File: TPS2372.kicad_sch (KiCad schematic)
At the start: 29 parts

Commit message: tps2372 finish
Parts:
- added C? (x4): 1nF, symbol Device:C
- added C?: 0.1uF, symbol Device:C
- added C?: 100uF, symbol Device:C_Polarized
- added C?: 47uF, symbol Device:C_Polarized
- added D?: 58V, symbol Device:D_TVS
- added D? (x3): Yellow, symbol Device:LED_Small
- added D?: D, symbol Device:D
- added D?: 100V, symbol Device:D_Schottky
- added D?: 12V, symbol Device:D_Zener
- added FB? (x4): 300ohm@100MHz, symbol Device:FerriteBead
- added J? (x3): Conn_01x02, TestPoint:TestPoint_2Pads_Pitch2.54mm_Drill0.8mm, symbol Connector_Generic:Conn_01x02
- added J?: Conn_01x03, symbol Connector_Generic:Conn_01x03
- added J?: Conn_02x05_Odd_Even, symbol Connector_Generic:Conn_02x05_Odd_Even
- added J?: Conn_02x02_Odd_Even, symbol Connector_Generic:Conn_02x02_Odd_Even
- added J?: Screw_Terminal_01x02, symbol Connector:Screw_Terminal_01x02
- added J?: Conn_01x02, symbol Connector_Generic:Conn_01x02
- added L? (x2): L_Coupled_1243, symbol Device:L_Coupled_1243
- added R?: 249, symbol Device:R
- added R?: 24.9k, symbol Device:R
- added R? (x3): 21k, symbol Device:R_Small
- added R? (x2): 49.9k, symbol Device:R
- added R?: 1k, symbol Device:R
- added R? (x2): 20k, symbol Device:R
- added R? (x2): 90.9, symbol Device:R
- added R?: 140, symbol Device:R
- added R? (x2): 63.4, symbol Device:R
- added R?: 53.6k, symbol Device:R
- added R?: 1.21k, symbol Device:R
- added RV?: 2k, symbol Device:R_Potentiometer
- added TP?: VSSA, symbol Connector:TestPoint
- added TP?: +48 Test 2, symbol Connector:TestPoint
- added TP?: AMPS_CTL, symbol Connector:TestPoint
- added TP? (x4): TestPoint, symbol Connector:TestPoint
- added TP?: RTN, symbol Connector:TestPoint
- added TP?: +48 Test 1, symbol Connector:TestPoint
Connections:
- net +48V: now also U?.1 (VDD), C?.1, C?.1, C?.1, C?.1, D?.1 (A1), D?.1 (K), FB?.2, L?.1, R?.1, R?.1, R?.2, R?.2, R?.2, TP?.1, TP?.1
- net BR_OFF: now also R?.1, R?.2
- net TCTA: now also C?.1, FB?.1, L?.2
- net TCTC: now also C?.2, FB?.1, L?.3
- net at U?.10 (AUTCLS_N): now also J?.1 (Pin_1)
- net PoE_RTN: now reaches U?.11 (RTN)
- net PoE_RTN: now also U?.12 (RTN), C?.2, C?.2, C?.2, D?.1 (K), FB?.2, J?.2 (Pin_2), L?.4, TP?.1
- net at U?.13 (PG): now also R?.2, TP?.1
- net at U?.16 (IRSHDL_EN): now also J?.1 (Pin_1)
- net at U?.17 (TPL): now also D?.1 (K), TP?.1
- net at U?.18 (TPH): now also D?.1 (K), TP?.1
- net at U?.19 (BT_N): now also D?.1 (K), TP?.1
- net at U?.2 (DEN): now also R?.2
- net at U?.21 (VSS): now also U?.4 (VSS), U?.5 (VSS), C?.2, J?.1 (Pin_1), J?.1 (Pin_1), J?.2 (Pin_2), J?.2 (Pin_2), J?.2 (Pin_2), J?.3 (Pin_3), J?.3 (Pin_3), J?.3 (Pin_3), J?.5 (Pin_5), J?.7 (Pin_7), J?.9 (Pin_9), R?.2, R?.2
- net at U?.3 (CLSA): now also R?.1, R?.1
- net at U?.6 (CLSB): now also R?.1, R?.1, R?.1, R?.1, R?.1
- net at U?.7 (REF): now also R?.1
- net at U?.8 (AMPS_CTL): now also R?.1, TP?.1
- net at U?.9 (MPS_DUTY): now also J?.2 (Pin_2)
- net at U?.5 (OUTP), U?.6 (OUTP), U?.7 (OUTP)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: no longer U?.5 (OUTP), U?.6 (OUTP), U?.7 (OUTP), U?.8 (OUTP)
- new net: J?.6 (Pin_6), R?.2
- new net: C?.2, FB?.1, J?.2 (Pin_2), L?.3
- new net: D?.2 (A), R?.1 (x4)
- new net: J?.1 (Pin_1), RV?.2
- new net: R?.2, RV?.3
- new net: J?.1 (Pin_1), R?.1
- new net: C?.1, D?.1 (K), D?.2 (A), FB?.2, L?.1
- new net: C?.1, FB?.1, J?.1 (Pin_1), L?.2
- new net: U?.5 (OUTP), U?.6 (OUTP), U?.7 (OUTP), U?.8 (OUTP)
- new net: J?.10 (Pin_10), R?.2
- new net: J?.2 (Pin_2), R?.2 (x2)
- new net: J?.4 (Pin_4), R?.2 (x2)
- new net: J?.8 (Pin_8), R?.2
- new net: D?.2 (A), R?.2
- new net VSSA: C?.2, D?.2 (A2), FB?.2, J?.1 (Pin_1), L?.4, TP?.1
- no-connect marks 0 -> 3
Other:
- note added: "4-Pair"
- note added: "Class 4 Class 3"
- note added: "Class 8 Class 7 Class 6 Class 5 Class 4"
- moved on the sheet: U?

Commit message: buck converter init
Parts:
- J?: footprint (none) -> TestPoint:TestPoint_2Pads_Pitch2.54mm_Drill0.8mm
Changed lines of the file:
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@@
       (effects (font (size 1.27 1.27)) (justify right))
     )
-    (property "Footprint" "" (id 2) (at 41.91 234.95 0)
+    (property "Footprint" "TestPoint:TestPoint_2Pads_Pitch2.54mm_Drill0.8mm" (id 2) (at 41.91 234.95 0)
       (effects (font (size 1.27 1.27)) hide)
     )

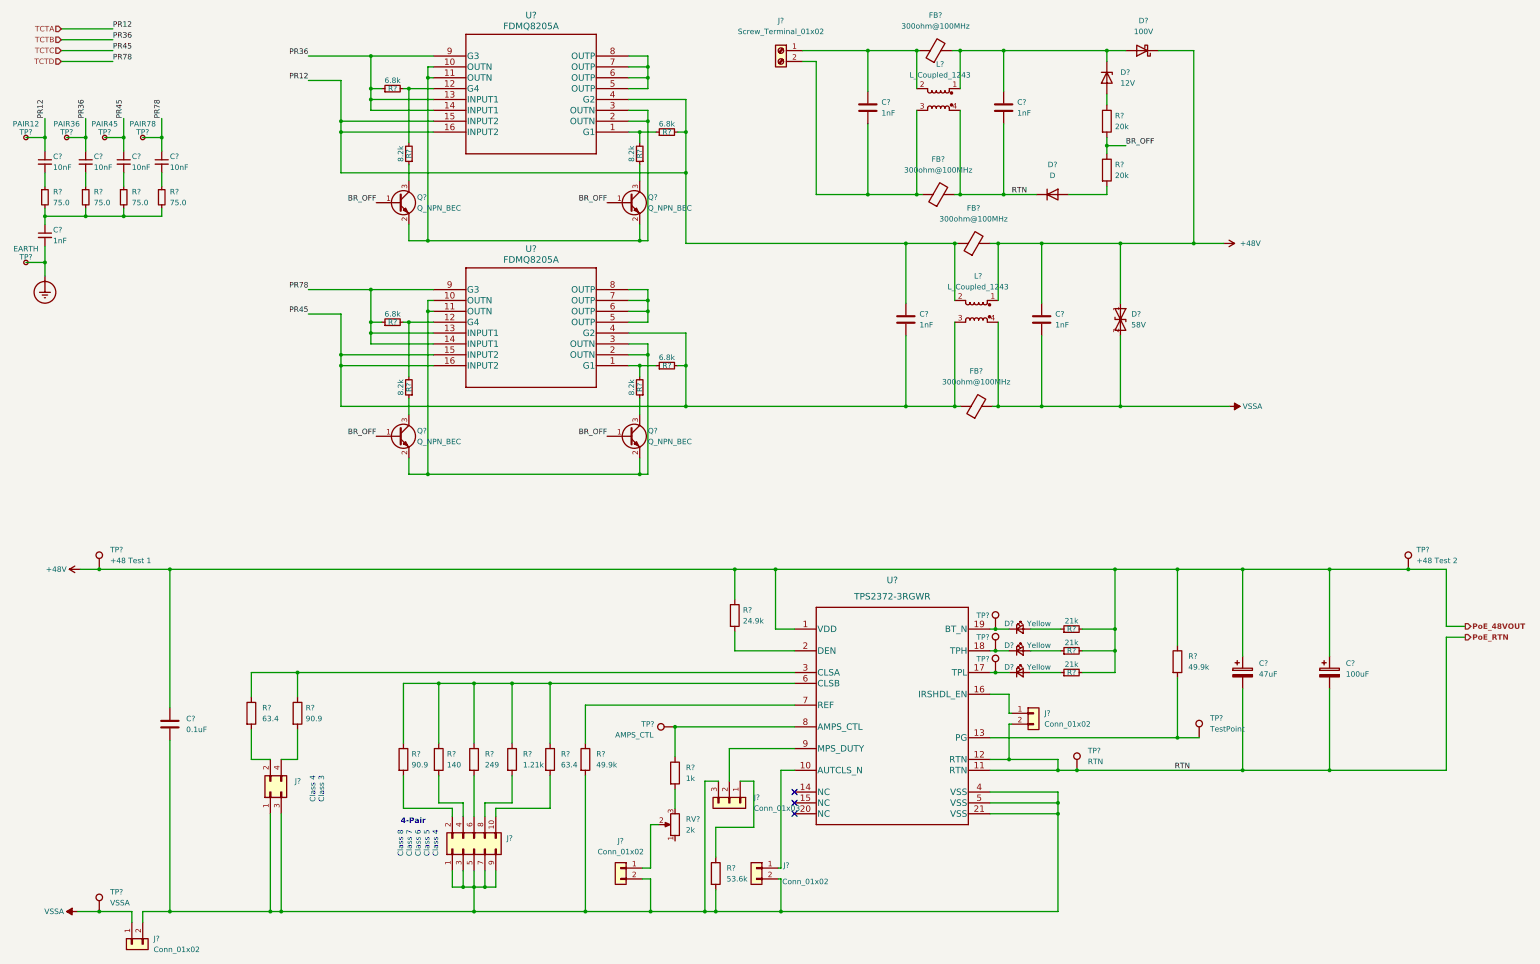
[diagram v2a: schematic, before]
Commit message: TPS2372 Modified, test jumpers removed
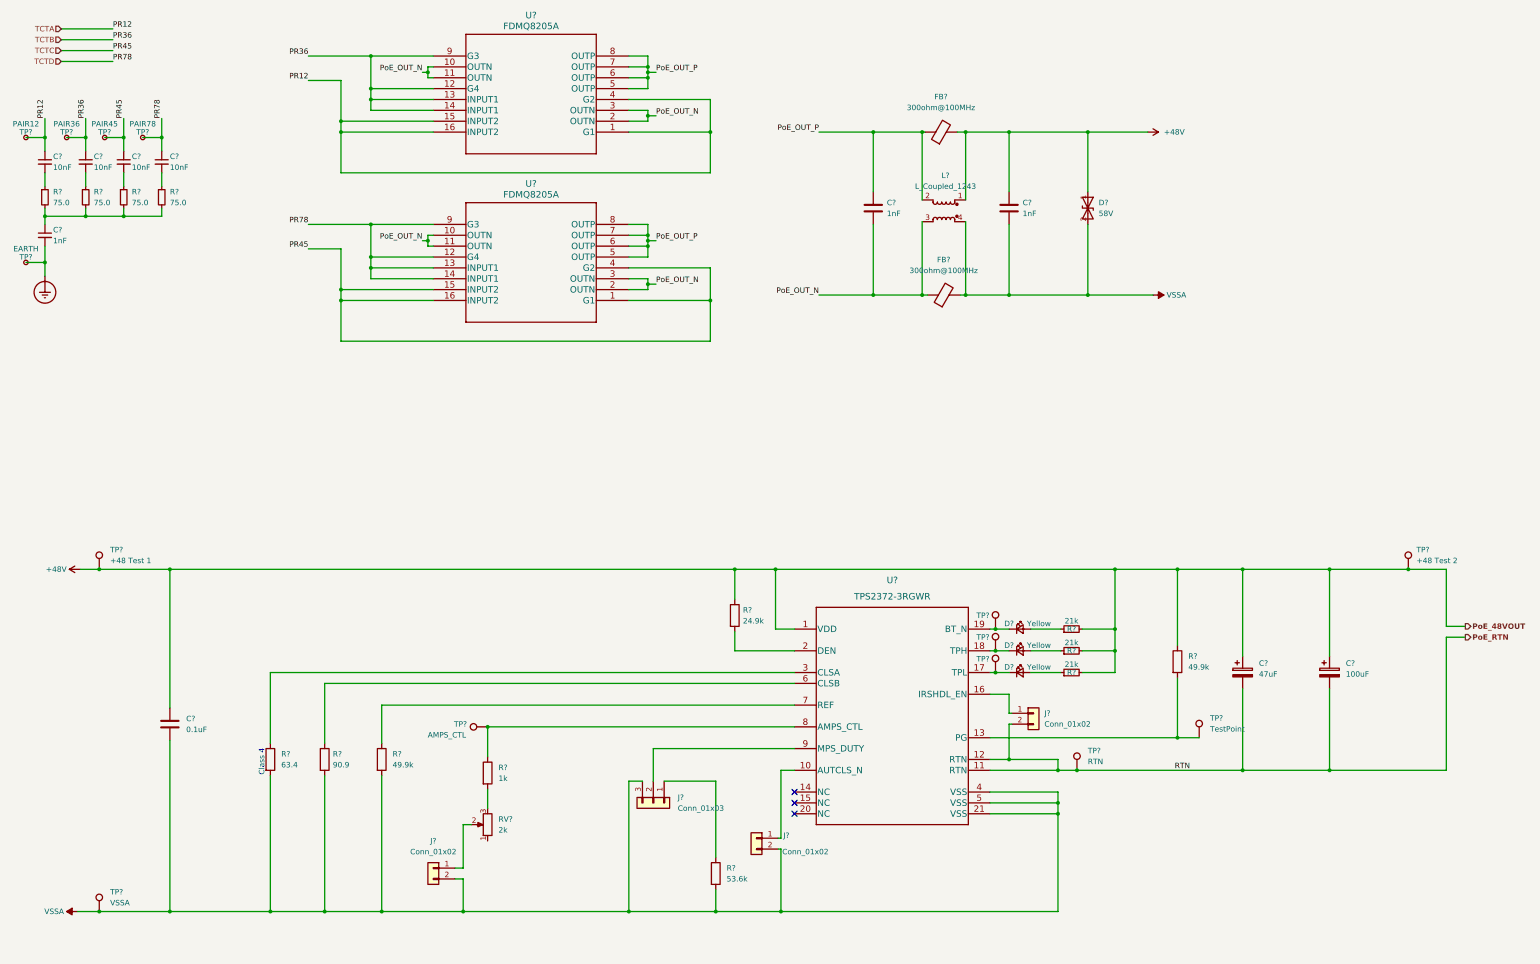
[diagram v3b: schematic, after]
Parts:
- removed C? (x2): 1nF, symbol Device:C
- removed D?: D, symbol Device:D
- removed D?: 100V, symbol Device:D_Schottky
- removed D?: 12V, symbol Device:D_Zener
- removed FB? (x2): 300ohm@100MHz, symbol Device:FerriteBead
- removed J?: Conn_02x05_Odd_Even, symbol Connector_Generic:Conn_02x05_Odd_Even
- removed J?: Conn_02x02_Odd_Even, symbol Connector_Generic:Conn_02x02_Odd_Even
- removed J?: Screw_Terminal_01x02, symbol Connector:Screw_Terminal_01x02
- removed J?: Conn_01x02, TestPoint:TestPoint_2Pads_Pitch2.54mm_Drill0.8mm, symbol Connector_Generic:Conn_01x02
- removed L?: L_Coupled_1243, symbol Device:L_Coupled_1243
- removed Q? (x4): Q_NPN_BEC, symbol Device:Q_NPN_BEC
- removed R?: 249, symbol Device:R
- removed R? (x4): 6.8k, symbol Device:R_Small
- removed R? (x4): 8.2k, symbol Device:R_Small
- removed R? (x2): 20k, symbol Device:R
- removed R?: 140, symbol Device:R
- removed R?: 63.4, symbol Device:R
- removed R?: 1.21k, symbol Device:R
- removed R?: 90.9, symbol Device:R
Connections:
- net TCTA: now also U?.1 (G1); no longer C?.1, FB?.1, L?.2
- net TCTB: now also U?.12 (G4)
- net TCTC: now also U?.1 (G1); no longer C?.2, FB?.1, L?.3
- net TCTD: now also U?.12 (G4)
- net VSSA: now also C?.2, J?.2 (Pin_2), J?.2 (Pin_2), J?.3 (Pin_3), R?.2, R?.2, R?.2, R?.2, U?.21 (VSS), U?.4 (VSS), U?.5 (VSS)
- net PoE_OUT_N: now reaches U?.10 (OUTN), U?.11 (OUTN), U?.2 (OUTN), U?.3 (OUTN)
- net PoE_OUT_N: now also C?.2, FB?.1, L?.3, U?.10 (OUTN), U?.11 (OUTN), U?.2 (OUTN), U?.3 (OUTN)
- net PoE_OUT_P: now reaches U?.5 (OUTP), U?.6 (OUTP), U?.7 (OUTP), U?.8 (OUTP)
- net PoE_OUT_P: now also C?.1, FB?.1, L?.2, U?.5 (OUTP), U?.6 (OUTP), U?.7 (OUTP), U?.8 (OUTP)
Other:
- note added: "Class 4"
- note removed: "4-Pair"
- note removed: "Class 4 Class 3"
- note removed: "Class 8 Class 7 Class 6 Class 5 Class 4"
- moved on the sheet: C?, D?, FB?, J?, L?, R?, RV?, TP?, U?

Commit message: PoE TR change to 7490220122; updated pwr net
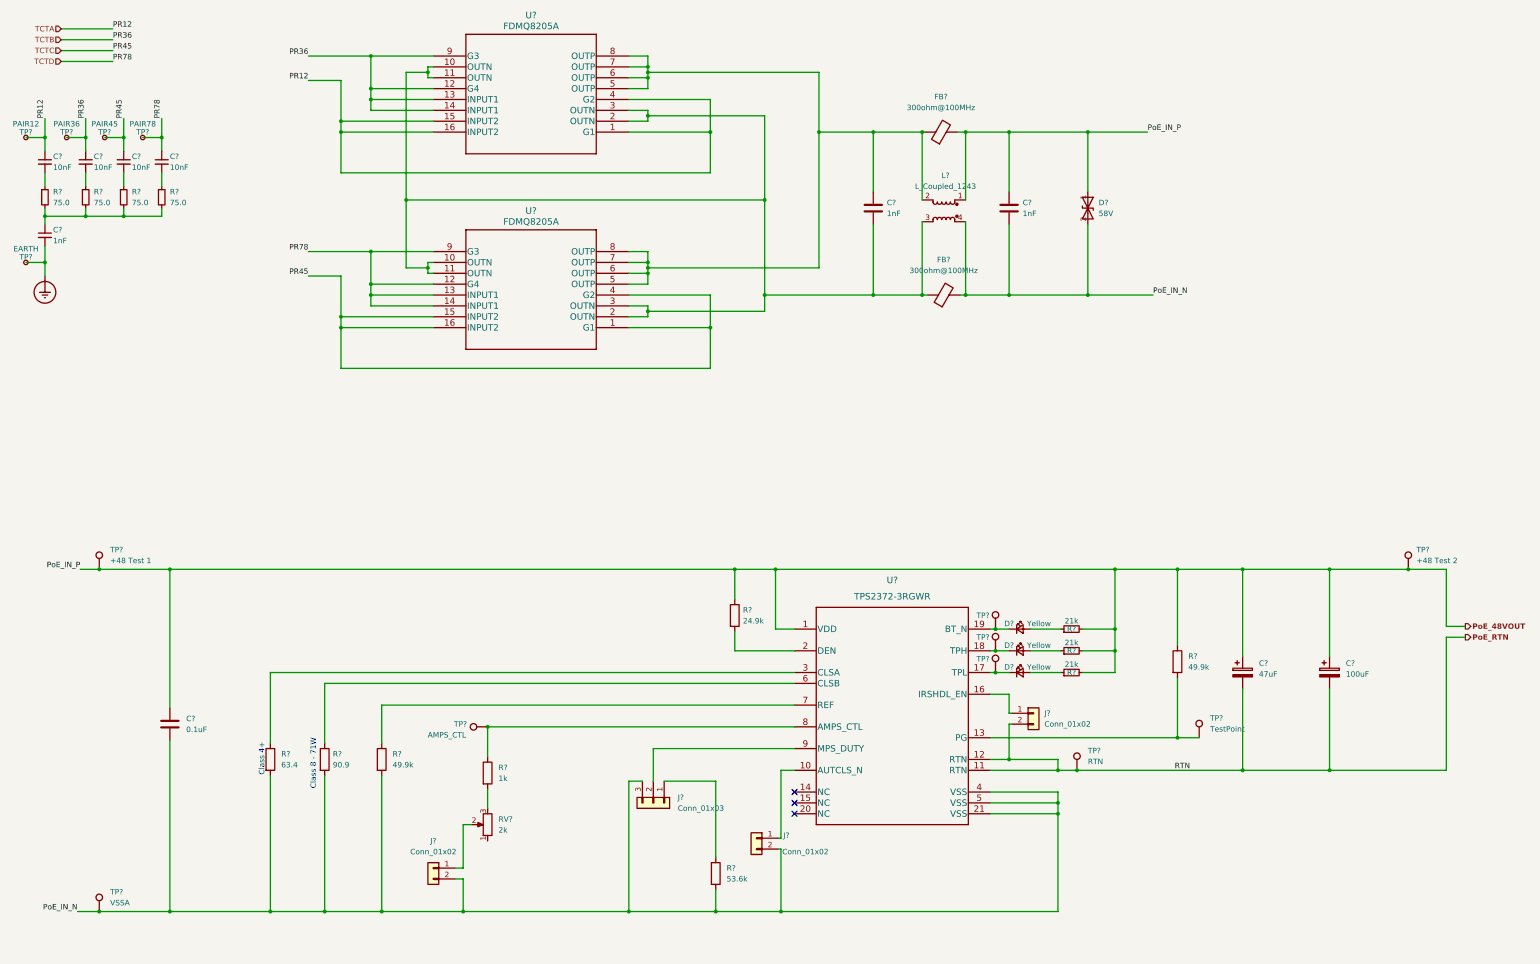
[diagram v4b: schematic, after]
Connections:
- net +48V renamed PoE_48VOUT
- net PoE_OUT_N: no longer names the net of C?.2, FB?.1, L?.3, U?.10 (OUTN), U?.10 (OUTN), U?.11 (OUTN), U?.11 (OUTN), U?.2 (OUTN), U?.2 (OUTN), U?.3 (OUTN), U?.3 (OUTN)
- net PoE_OUT_P: no longer names the net of C?.1, FB?.1, L?.2, U?.5 (OUTP), U?.5 (OUTP), U?.6 (OUTP), U?.6 (OUTP), U?.7 (OUTP), U?.7 (OUTP), U?.8 (OUTP), U?.8 (OUTP)
- net VSSA renamed PoE_IN_N
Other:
- note added: "Class 4+"
- note added: "Class 8 - 71W"
- note removed: "Class 4"
- moved on the sheet: U?

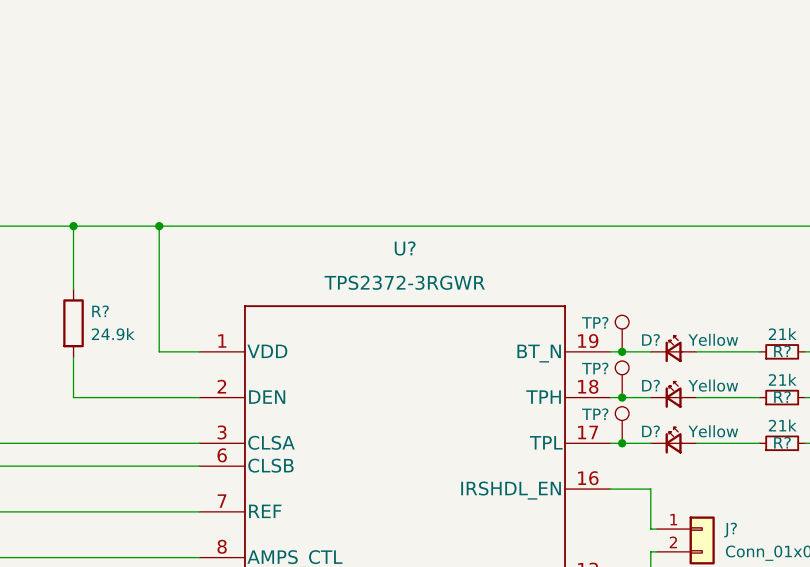
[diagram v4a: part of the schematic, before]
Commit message: LM2575 added, provide 3V3
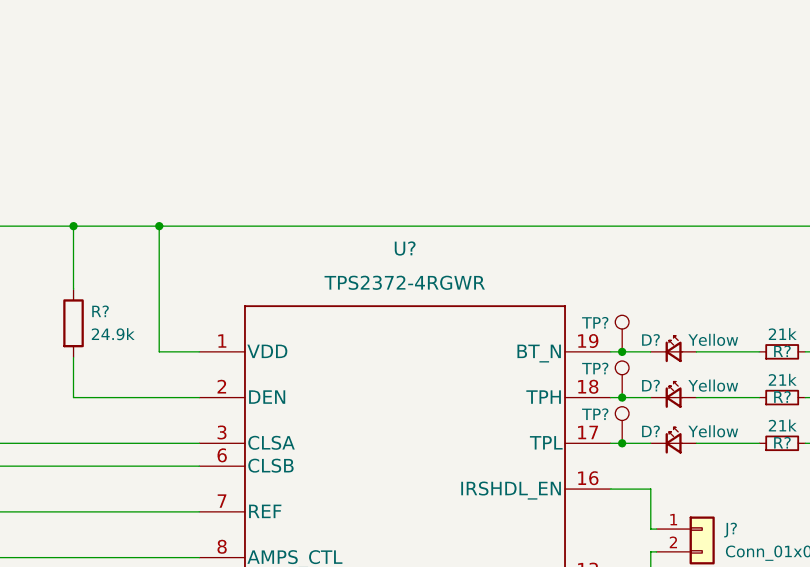
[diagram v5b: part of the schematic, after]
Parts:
- U?: value TPS2372-3RGWR -> TPS2372-4RGWR
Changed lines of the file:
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@@
       (effects (font (size 1.524 1.524)))
     )
-    (property "Value" "TPS2372-3RGWR" (id 1) (at 219.71 153.67 0)
+    (property "Value" "TPS2372-4RGWR" (id 1) (at 219.71 153.67 0)
       (effects (font (size 1.524 1.524)))
     )
